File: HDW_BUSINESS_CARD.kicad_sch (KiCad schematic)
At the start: 5 parts, among them U1 NT3H1101_NT3H1201

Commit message: ready for NFC coil development
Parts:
- added C2: 440nF, Capacitor_SMD:C_0603_1608Metric_Pad1.05x0.95mm_HandSolder, symbol business card-rescue:CAP-pspice
- L1: value 2.75uH -> 1.64uH
- U1: value NT3H1101_NT3H1201 -> NT3H1101
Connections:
- net at L1.1, U1.1 (LA): now also C2.2
- net at L1.2, U1.8 (LB): now also C2.1
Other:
- moved on the sheet: L1
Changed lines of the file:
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@@
 	(paper "A4")
+	(junction
+		(at 129.54 81.28)
+		(diameter 0)
+		(color 0 0 0 0)
+	)
 	(junction
 		(at 156.21 106.68)
@@
 	)
 	(junction
+		(at 156.21 81.28)
+		(diameter 0)
+		(color 0 0 0 0)
+	)
+	(junction
 		(at 129.54 120.65)
 		(diameter 0)
@@
 	(wire
 		(pts
-			(xy 160.02 88.9) (xy 160.02 91.44)
-		)
-		(stroke
-			(width 0)
-			(type default)
-		)
-	)
-	(wire
-		(pts
 			(xy 160.02 120.65) (xy 160.02 106.68)
 		)
@@
 	(wire
 		(pts
+			(xy 147.32 66.04) (xy 156.21 66.04)
+		)
+		(stroke
+			(width 0)
+			(type default)
+		)
+	)
+	(wire
+		(pts
+			(xy 129.54 66.04) (xy 129.54 81.28)
+		)
+		(stroke
+			(width 0)
+			(type default)
+		)
+	)
+	(wire
+		(pts
 			(xy 133.35 130.81) (xy 129.54 130.81)
 		)
@@
 	(wire
 		(pts
+			(xy 156.21 81.28) (xy 156.21 99.06)
+		)
+		(stroke
+			(width 0)
+			(type default)
+		)
+	)
+	(wire
+		(pts
 			(xy 129.54 120.65) (xy 138.43 120.65)
 		)
@@
 	(wire
 		(pts
+			(xy 156.21 99.06) (xy 153.67 99.06)
+		)
+		(stroke
+			(width 0)
+			(type default)
+		)
+	)
+	(wire
+		(pts
 			(xy 129.54 130.81) (xy 129.54 120.65)
 		)
@@
 	(wire
 		(pts
+			(xy 129.54 66.04) (xy 139.7 66.04)
+		)
+		(stroke
+			(width 0)
+			(type default)
+		)
+	)
+	(wire
+		(pts
+			(xy 149.86 81.28) (xy 156.21 81.28)
+		)
+		(stroke
+			(width 0)
+			(type default)
+		)
+	)
+	(wire
+		(pts
+			(xy 156.21 66.04) (xy 156.21 81.28)
+		)
+		(stroke
+			(width 0)
+			(type default)
+		)
+	)
+	(wire
+		(pts
 			(xy 144.78 130.81) (xy 140.97 130.81)
 		)
@@
 	(wire
 		(pts
-			(xy 160.02 99.06) (xy 153.67 99.06)
-		)
-		(stroke
-			(width 0)
-			(type default)
-		)
-	)
-	(wire
-		(pts
-			(xy 129.54 88.9) (xy 160.02 88.9)
+			(xy 129.54 81.28) (xy 137.16 81.28)
 		)
 		(stroke
@@
 	(wire
 		(pts
-			(xy 129.54 99.06) (xy 129.54 88.9)
+			(xy 129.54 99.06) (xy 129.54 81.28)
 		)
 		(stroke
@@
 			(width 0)
 			(type default)
+		)
+	)
+	(text_box "NT3H1101 parallel capacitance is 50pF\n\nIgnoring antenna capacitance, to get a \nresonant frequency of 13.56MHz, we need \nan inductance of 2.77518uH"
+		(exclude_from_sim no)
+		(at 44.45 27.94 0)
+		(size 44.45 16.51)
+		(stroke
+			(width 0)
+			(type default)
+		)
+		(fill
+			(type none)
+		)
+		(effects
+			(font
+				(size 1.27 1.27)
+			)
+			(justify left top)
 		)
 	)
@@
 			)
 		)
-		(property "Value" "NT3H1101_NT3H1201"
+		(property "Value" "NT3H1101"
 			(at 144.78 93.98 0)
 			(effects
@@
 	(symbol
 		(lib_id "Device:L")
-		(at 160.02 95.25 0)
+		(at 143.51 66.04 90)
 		(unit 1)
 		(exclude_from_sim no)
@@
 		(dnp no)
 		(property "Reference" "L1"
-			(at 161.3408 94.0816 0)
-			(effects
-				(font
-					(size 1.27 1.27)
-				)
-				(justify left)
-			)
-		)
-		(property "Value" "2.75uH"
-			(at 161.3408 96.393 0)
+			(at 142.3416 64.7192 0)
+			(effects
+				(font
+					(size 1.27 1.27)
+				)
+				(justify left)
+			)
+		)
+		(property "Value" "1.64uH"
+			(at 144.653 64.7192 0)
 			(effects
 				(font
@@
 		)
 		(property "Footprint" ""
-			(at 160.02 95.25 0)
+			(at 143.51 66.04 0)
 			(effects
 				(font
@@
 		)
 		(property "Datasheet" "~"
-			(at 160.02 95.25 0)
-			(effects
-				(font
-					(size 1.27 1.27)
-				)
-				(hide yes)
-			)
-		)
-		(property "Description" ""
-			(at 160.02 95.25 0)
-			(effects
-				(font
-					(size 1.27 1.27)
-				)
-				(hide yes)
+			(at 143.51 66.04 0)
+			(effects
+				(font
+					(size 1.27 1.27)
+				)
+				(hide yes)
+			)
+		)
+		(property "Description" "Antenna"
+			(at 144.018 67.564 90)
+			(effects
+				(font
+					(size 1.27 1.27)
+				)
 			)
 		)
@@
 					(unit 1)
 				)
+			)
+		)
+	)
+	(symbol
+		(lib_id "business card-rescue:CAP-pspice")
+		(at 143.51 81.28 270)
+		(unit 1)
+		(exclude_from_sim no)
+		(in_bom yes)
+		(on_board yes)
+		(dnp no)
+		(property "Reference" "C2"
+			(at 146.05 83.82 90)
+			(effects
+				(font
+					(size 1.27 1.27)
+				)
+				(justify left)
+			)
+		)
+		(property "Value" "440nF"
+			(at 146.05 86.36 90)
+			(effects
+				(font
+					(size 1.27 1.27)
+				)
+				(justify left)
+			)
+		)
+		(property "Footprint" "Capacitor_SMD:C_0603_1608Metric_Pad1.05x0.95mm_HandSolder"
+			(at 143.51 81.28 0)
+			(effects
+				(font
+					(size 1.27 1.27)
+				)
+				(hide yes)
+			)
+		)
+		(property "Datasheet" "~"
+			(at 143.51 81.28 0)
+			(effects
+				(font
+					(size 1.27 1.27)
+				)
+				(hide yes)
+			)
+		)
+		(property "Description" "Tunig Capacitor"
+			(at 143.51 75.946 90)
+			(effects
+				(font
+					(size 1.27 1.27)
+				)
+			)
+		)
+		(pin "1"
+		)
+		(pin "2"
+		)
+		(instances
+			(project "HDW_BUSINESS_CARD"
+				(path "/4902e220-27e2-4a10-86d3-f5ff54ae57f8"
+					(reference "C2")
+					(unit 1)
+				)

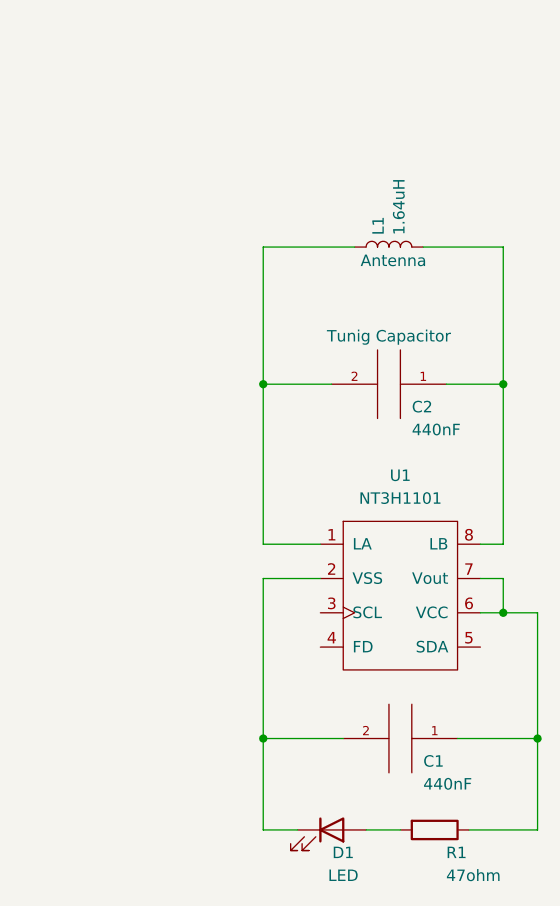
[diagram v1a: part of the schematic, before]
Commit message: submitted to PCBWay, still need to update BOM with proper components and PCB coil
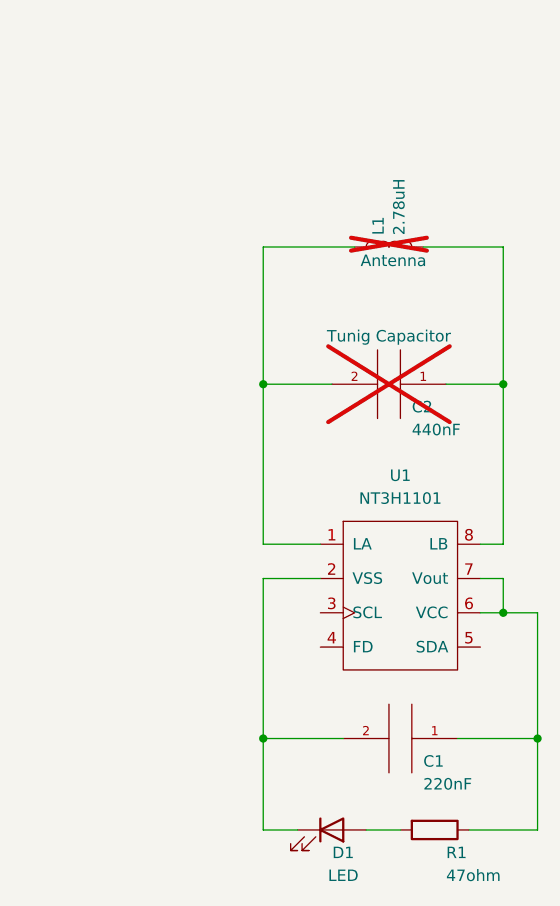
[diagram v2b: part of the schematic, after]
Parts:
- C1: value 440nF -> 220nF; footprint Capacitor_SMD:C_0603_1608Metric_Pad1.05x0.95mm_HandSolder -> Capacitor_SMD:C_0402_1005Metric
- C2: footprint Capacitor_SMD:C_0603_1608Metric_Pad1.05x0.95mm_HandSolder -> Capacitor_SMD:C_0603_1608Metric_Pad1.08x0.95mm_HandSolder; now not fitted
- D1: footprint (none) -> Diode_SMD:D_0805_2012Metric; MFG_PART_NUMBER (none) -> 150080RS75000
- L1: value 1.64uH -> 2.78uH; now not fitted
- R1: footprint Resistor_SMD:R_0603_1608Metric_Pad1.05x0.95mm_HandSolder -> Capacitor_SMD:C_0402_1005Metric
- U1: MFG_PART (none) -> NT3H1101; MFG_PART_NUMBER (none) -> NT3H1101
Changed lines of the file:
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@@
 			)
 		)
-		(property "Value" "440nF"
+		(property "Value" "220nF"
 			(at 147.32 125.73 90)
 			(effects
@@
 			)
 		)
-		(property "Footprint" "Capacitor_SMD:C_0603_1608Metric_Pad1.05x0.95mm_HandSolder"
+		(property "Footprint" "Capacitor_SMD:C_0402_1005Metric"
 			(at 144.78 120.65 0)
 			(effects
@@
 			)
 		)
-		(property "Footprint" "Resistor_SMD:R_0603_1608Metric_Pad1.05x0.95mm_HandSolder"
+		(property "Footprint" "Capacitor_SMD:C_0402_1005Metric"
 			(at 148.59 129.032 90)
 			(effects
@@
 			)
 		)
-		(property "Footprint" ""
+		(property "Footprint" "Diode_SMD:D_0805_2012Metric"
 			(at 137.16 130.81 0)
 			(effects
@@
 		)
 		(property "Description" ""
+			(at 137.16 130.81 0)
+			(effects
+				(font
+					(size 1.27 1.27)
+				)
+				(hide yes)
+			)
+		)
+		(property "MFG_PART_NUMBER" "150080RS75000"
 			(at 137.16 130.81 0)
 			(effects
@@
 			)
 		)
+		(property "MFG_PART" "NT3H1101"
+			(at 144.78 105.41 0)
+			(effects
+				(font
+					(size 1.27 1.27)
+				)
+				(hide yes)
+			)
+		)
+		(property "MFG_PART_NUMBER" "NT3H1101"
+			(at 144.78 105.41 0)
+			(effects
+				(font
+					(size 1.27 1.27)
+				)
+				(hide yes)
+			)
+		)
 		(pin "5"
 		)
@@
 		(in_bom yes)
 		(on_board yes)
-		(dnp no)
+		(dnp yes)
 		(property "Reference" "L1"
 			(at 142.3416 64.7192 0)
@@
 			)
 		)
-		(property "Value" "1.64uH"
+		(property "Value" "2.78uH"
 			(at 144.653 64.7192 0)
 			(effects
@@
 		(in_bom yes)
 		(on_board yes)
-		(dnp no)
+		(dnp yes)
 		(property "Reference" "C2"
 			(at 146.05 83.82 90)
@@
 			)
 		)
-		(property "Footprint" "Capacitor_SMD:C_0603_1608Metric_Pad1.05x0.95mm_HandSolder"
+		(property "Footprint" "Capacitor_SMD:C_0603_1608Metric_Pad1.08x0.95mm_HandSolder"
 			(at 143.51 81.28 0)
 			(effects

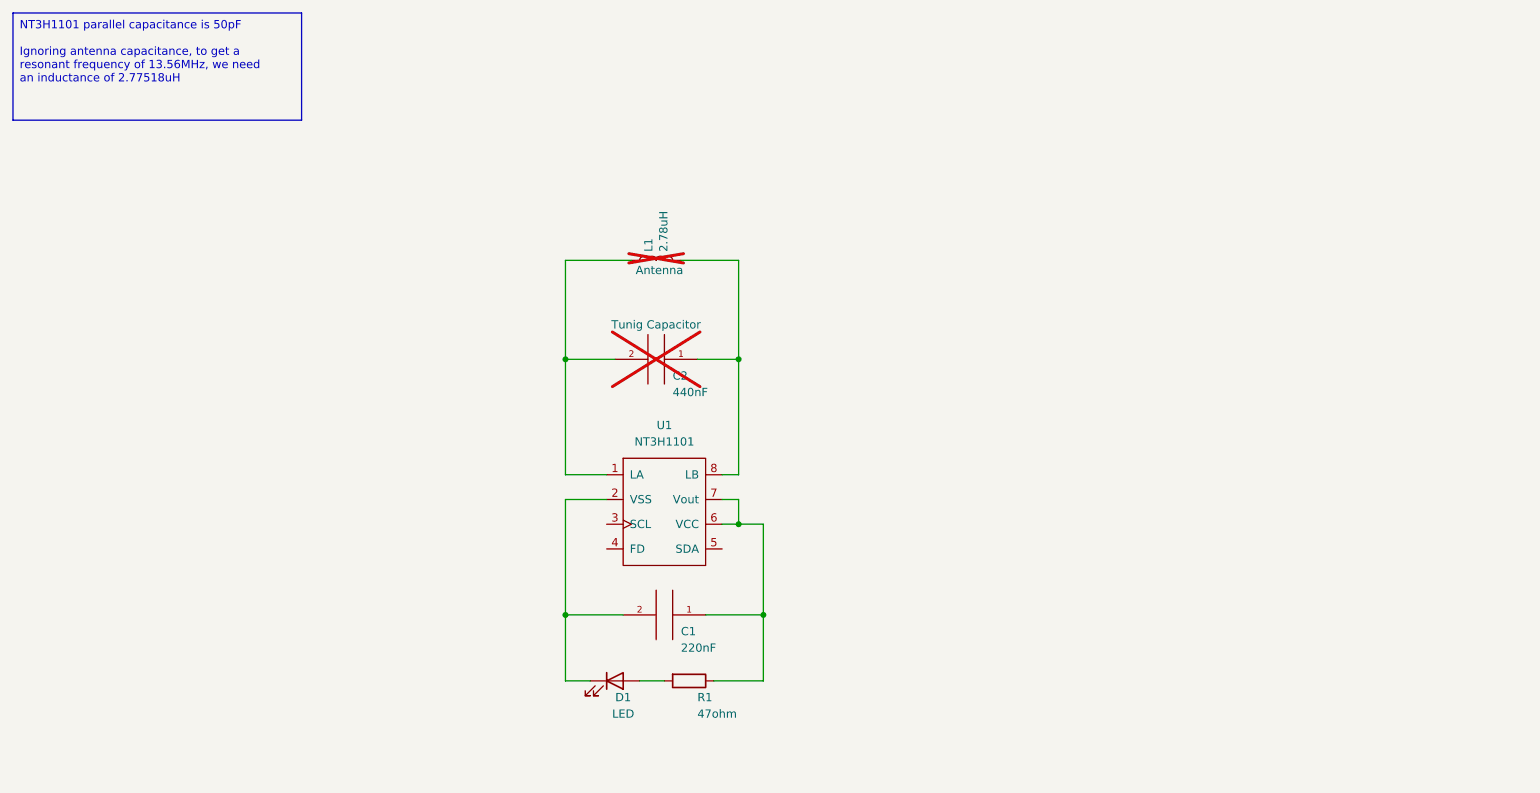
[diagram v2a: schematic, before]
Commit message: setup hex coil nets
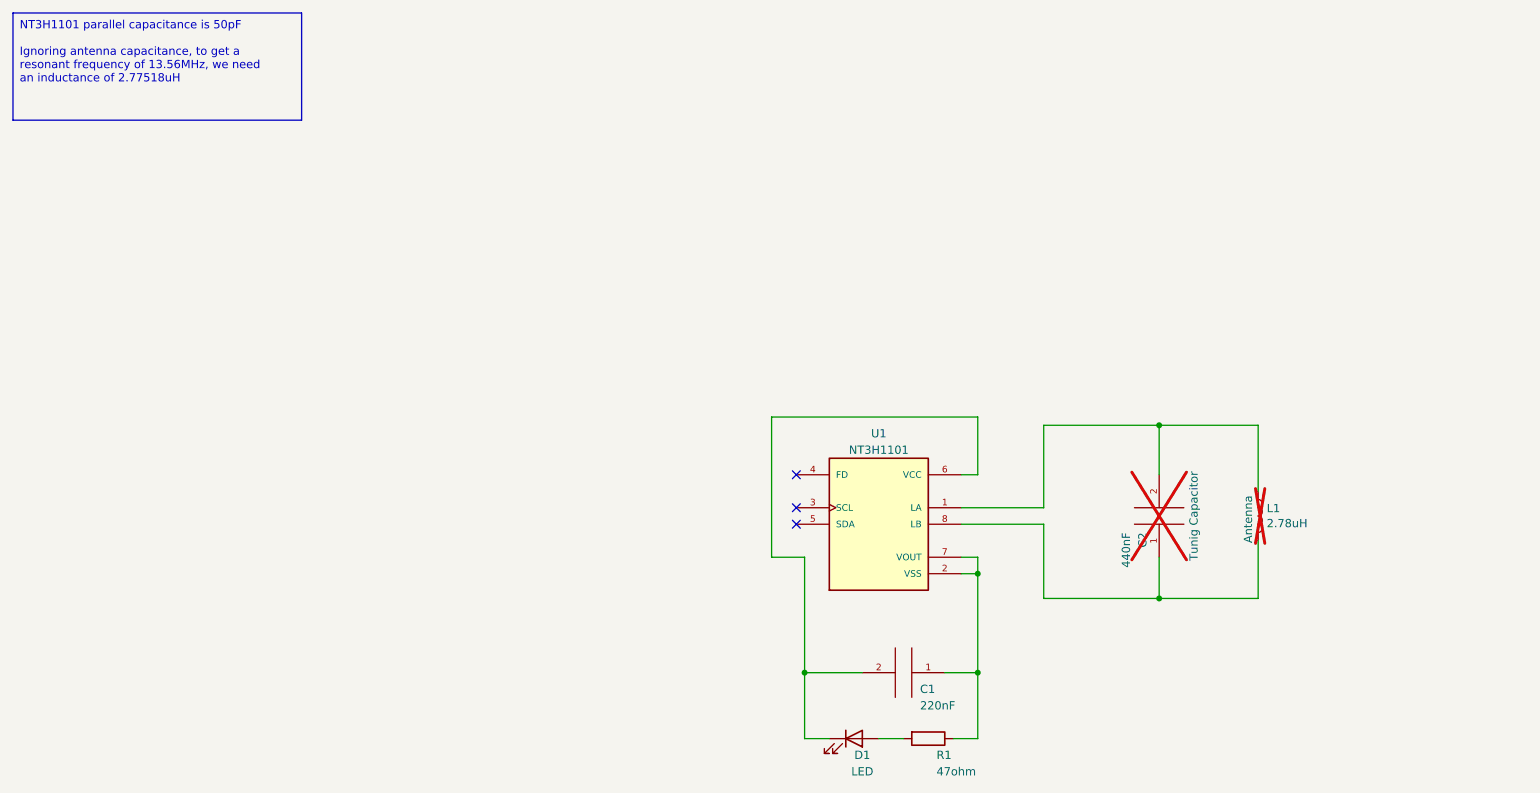
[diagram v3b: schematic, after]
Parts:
- U1: footprint Package_SO:TSSOP-8_4.4x3mm_P0.65mm -> Lechnology Footprints Library:QFN8P50_160X160X50L40X20N; symbol business card-rescue:NT3H1101_NT3H1201-MCU_NXP_NT3H11 -> NT3H2111W0FHKH:NT3H2111W0FHKH; MANUFACTURER (none) -> NXP Semiconductors
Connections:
- net at C1.1, R1.1, U1.7 (VOUT): now also U1.2 (VSS); no longer U1.6 (VCC)
- net at C1.2, D1.1 (K): now also U1.6 (VCC); no longer U1.2 (VSS)
- no-connect marks 0 -> 3
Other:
- moved on the sheet: C1, C2, D1, L1, R1

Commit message: sending off to PCBWay for first order
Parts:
- C1: LCSC (none) -> C915854; MFG_PART_NUMBER (none) -> TCC0402X7R224K250AT
- D1: LCSC (none) -> C19192157
- R1: LCSC (none) -> C137973; MFG_PART_NUMBER (none) -> RC0402FR-0747RL
- U1: LCSC (none) -> C73156; MFG_PART NT3H1101 -> (none); MFG_PART_NUMBER NT3H1101 -> NT3H2111W0 FHKH
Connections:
- net at C1.1, R1.1, U1.7 (VOUT): now also U1.6 (VCC); no longer U1.2 (VSS)
- net at C1.2, D1.1 (K): now also U1.2 (VSS); no longer U1.6 (VCC)
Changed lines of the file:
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@@
+	)
+	(junction
+		(at 193.04 129.54)
+		(diameter 0)
+		(color 0 0 0 0)
+	)
+	(junction
+		(at 161.29 129.54)
+		(diameter 0)
+		(color 0 0 0 0)
+	)
+	(junction
+		(at 193.04 111.76)
+		(diameter 0)
+		(color 0 0 0 0)
 	)
 	(junction
@@
 		(color 0 0 0 0)
 	)
-	(junction
-		(at 193.04 114.3)
-		(diameter 0)
-		(color 0 0 0 0)
-	)
-	(junction
-		(at 166.37 129.54)
-		(diameter 0)
-		(color 0 0 0 0)
-	)
-	(junction
-		(at 193.04 129.54)
-		(diameter 0)
-		(color 0 0 0 0)
-	)
 	(no_connect
 		(at 165.1 99.06)
@@
 	(wire
 		(pts
-			(xy 193.04 114.3) (xy 190.5 114.3)
-		)
-		(stroke
-			(width 0)
-			(type default)
-		)
-	)
-	(wire
-		(pts
-			(xy 193.04 129.54) (xy 193.04 114.3)
-		)
-		(stroke
-			(width 0)
-			(type default)
-		)
-	)
-	(wire
-		(pts
 			(xy 236.22 109.22) (xy 236.22 118.11)
 		)
@@
 	(wire
 		(pts
-			(xy 170.18 139.7) (xy 166.37 139.7)
+			(xy 190.5 114.3) (xy 190.5 121.92)
+		)
+		(stroke
+			(width 0)
+			(type default)
+		)
+	)
+	(wire
+		(pts
+			(xy 193.04 111.76) (xy 193.04 129.54)
+		)
+		(stroke
+			(width 0)
+			(type default)
+		)
+	)
+	(wire
+		(pts
+			(xy 170.18 139.7) (xy 161.29 139.7)
+		)
+		(stroke
+			(width 0)
+			(type default)
+		)
+	)
+	(wire
+		(pts
+			(xy 161.29 121.92) (xy 161.29 129.54)
+		)
+		(stroke
+			(width 0)
+			(type default)
+		)
+	)
+	(wire
+		(pts
+			(xy 193.04 99.06) (xy 193.04 111.76)
+		)
+		(stroke
+			(width 0)
+			(type default)
+		)
+	)
+	(wire
+		(pts
+			(xy 220.98 118.11) (xy 203.2 118.11)
 		)
 		(stroke
@@
 	(wire
 		(pts
-			(xy 220.98 118.11) (xy 203.2 118.11)
-		)
-		(stroke
-			(width 0)
-			(type default)
-		)
-	)
-	(wire
-		(pts
-			(xy 166.37 129.54) (xy 175.26 129.54)
+			(xy 161.29 129.54) (xy 175.26 129.54)
 		)
 		(stroke
@@
 	(wire
 		(pts
-			(xy 166.37 139.7) (xy 166.37 129.54)
+			(xy 161.29 139.7) (xy 161.29 129.54)
 		)
 		(stroke
@@
 	(wire
 		(pts
-			(xy 193.04 90.17) (xy 161.29 90.17)
-		)
-		(stroke
-			(width 0)
-			(type default)
-		)
-	)
-	(wire
-		(pts
 			(xy 236.22 118.11) (xy 220.98 118.11)
 		)
@@
 	(wire
 		(pts
-			(xy 193.04 111.76) (xy 190.5 111.76)
-		)
-		(stroke
-			(width 0)
-			(type default)
-		)
-	)
-	(wire
-		(pts
 			(xy 220.98 91.44) (xy 220.98 99.06)
 		)
@@
 	(wire
 		(pts
-			(xy 161.29 90.17) (xy 161.29 111.76)
+			(xy 190.5 121.92) (xy 161.29 121.92)
 		)
 		(stroke
@@
 	(wire
 		(pts
-			(xy 193.04 99.06) (xy 193.04 90.17)
-		)
-		(stroke
-			(width 0)
-			(type default)
-		)
-	)
-	(wire
-		(pts
-			(xy 193.04 114.3) (xy 193.04 111.76)
-		)
-		(stroke
-			(width 0)
-			(type default)
-		)
-	)
-	(wire
-		(pts
 			(xy 189.23 139.7) (xy 193.04 139.7)
 		)
@@
 	(wire
 		(pts
-			(xy 166.37 111.76) (xy 166.37 129.54)
-		)
-		(stroke
-			(width 0)
-			(type default)
-		)
-	)
-	(wire
-		(pts
-			(xy 161.29 111.76) (xy 166.37 111.76)
-		)
-		(stroke
-			(width 0)
-			(type default)
+			(xy 190.5 111.76) (xy 193.04 111.76)
+		)
+		(stroke
+			(width 0)
+			(type default)
+		)
+	)
+	(text_box "Total coil resistance: 1.142585 Ohms\nTotal coil resistance: 2.774 uH  Ohms\nEstimated Coil Capacity: 2.0pF"
+		(exclude_from_sim no)
+		(at 231.14 123.19 0)
+		(size 45.72 12.7)
+		(stroke
+			(width 0)
+			(type default)
+		)
+		(fill
+			(type none)
+		)
+		(effects
+			(font
+				(size 1.27 1.27)
+			)
+			(justify left top)
 		)
 	)
@@
 			)
 		)
+		(property "LCSC" "C915854"
+			(at 181.61 129.54 0)
+			(effects
+				(font
+					(size 1.27 1.27)
+				)
+				(hide yes)
+			)
+		)
+		(property "MFG_PART_NUMBER" "TCC0402X7R224K250AT"
+			(at 181.61 129.54 0)
+			(effects
+				(font
+					(size 1.27 1.27)
+				)
+				(hide yes)
+			)
+		)
 		(pin "1"
 		)
@@
 			)
 		)
+		(property "LCSC" "C137973"
+			(at 185.42 139.7 0)
+			(effects
+				(font
+					(size 1.27 1.27)
+				)
+				(hide yes)
+			)
+		)
+		(property "MFG_PART_NUMBER" "RC0402FR-0747RL"
+			(at 185.42 139.7 0)
+			(effects
+				(font
+					(size 1.27 1.27)
+				)
+				(hide yes)
+			)
+		)
 		(pin "1"
 		)
@@
 			)
 		)
+		(property "LCSC" "C19192157"
+			(at 173.99 139.7 0)
+			(effects
+				(font
+					(size 1.27 1.27)
+				)
+				(hide yes)
+			)
+		)
 		(pin "2"
 		)
@@
 			)
 		)
-		(property "MFG_PART" "NT3H1101"
+		(property "MFG_PART" ""
 			(at 177.8 106.68 0)
 			(effects
@@
 			)
 		)
-		(property "MFG_PART_NUMBER" "NT3H1101"
+		(property "MFG_PART_NUMBER" "NT3H2111W0 FHKH"
 			(at 177.8 106.68 0)
 			(effects
@@
 				(hide yes)
 			)
+		)
+		(property "LCSC" "C73156"
+			(at 177.8 106.68 0)
+			(effects
+				(font
+					(size 1.27 1.27)
+				)
+				(hide yes)
+			)

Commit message: removed C2
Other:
- note added: "C2 is used to tune the first PCB Antenna iteration It is excluded from board for production runs"
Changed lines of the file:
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@@
 (kicad_sch
-	(version 20231120)
+	(version 20250114)
 	(generator "eeschema")
-	(generator_version "8.0")
+	(generator_version "9.0")
 	(paper "A4")
+	(text "C2 is used to tune the first PCB Antenna iteration\nIt is excluded from board for production runs"
+		(exclude_from_sim no)
+		(at 222.25 87.122 0)
+		(effects
+			(font
+				(size 1.27 1.27)
+				(thickness 0.254)
+				(bold yes)
+			)
+		)
+	)
+	(text_box "Total coil resistance: 1.142585 Ohms\nTotal coil resistance: 2.774 uH  Ohms\nEstimated Coil Capacity: 2.0pF"
+		(exclude_from_sim no)
+		(at 231.14 123.19 0)
+		(size 45.72 12.7)
+		(margins 0.9525 0.9525 0.9525 0.9525)
+		(stroke
+			(width 0)
+			(type default)
+		)
+		(fill
+			(type none)
+		)
+		(effects
+			(font
+				(size 1.27 1.27)
+			)
+			(justify left top)
+		)
+	)
+	(text_box "NT3H1101 parallel capacitance is 50pF\n\nIgnoring antenna capacitance, to get a \nresonant frequency of 13.56MHz, we need \nan inductance of 2.77518uH"
+		(exclude_from_sim no)
+		(at 44.45 27.94 0)
+		(size 44.45 16.51)
+		(margins 0.9525 0.9525 0.9525 0.9525)
+		(stroke
+			(width 0)
+			(type default)
+		)
+		(fill
+			(type none)
+		)
+		(effects
+			(font
+				(size 1.27 1.27)
+			)
+			(justify left top)
+		)
+	)
 	(junction
 		(at 220.98 91.44)
@@
 			(width 0)
 			(type default)
-		)
-	)
-	(text_box "Total coil resistance: 1.142585 Ohms\nTotal coil resistance: 2.774 uH  Ohms\nEstimated Coil Capacity: 2.0pF"
-		(exclude_from_sim no)
-		(at 231.14 123.19 0)
-		(size 45.72 12.7)
-		(stroke
-			(width 0)
-			(type default)
-		)
-		(fill
-			(type none)
-		)
-		(effects
-			(font
-				(size 1.27 1.27)
-			)
-			(justify left top)
-		)
-	)
-	(text_box "NT3H1101 parallel capacitance is 50pF\n\nIgnoring antenna capacitance, to get a \nresonant frequency of 13.56MHz, we need \nan inductance of 2.77518uH"
-		(exclude_from_sim no)
-		(at 44.45 27.94 0)
-		(size 44.45 16.51)
-		(stroke
-			(width 0)
-			(type default)
-		)
-		(fill
-			(type none)
-		)
-		(effects
-			(font
-				(size 1.27 1.27)
-			)
-			(justify left top)
 		)
 	)
@@
 		(exclude_from_sim no)
 		(in_bom yes)
-		(on_board yes)
+		(on_board no)
 		(dnp yes)
 		(property "Reference" "C2"
@@
 		)
 	)
+	(embedded_fonts no)
 )
